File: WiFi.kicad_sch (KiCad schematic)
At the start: 0 parts

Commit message: PMIC DCDC
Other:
- title: Leaf RV1126 Power -> Leaf RV1126 PMIC RK809
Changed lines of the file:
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@@
   (paper "A4")
   (title_block
-    (title "Leaf RV1126 Power")
+    (title "Leaf RV1126 PMIC RK809")
     (date "2023-02-23")
     (rev "1")

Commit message: updated: PMIC codec
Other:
- title: Leaf RV1126 PMIC RK809 -> Leaf RV1126 PMIC RK809 Codec
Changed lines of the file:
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@@
   (paper "A4")
   (title_block
-    (title "Leaf RV1126 PMIC RK809")
-    (date "2023-02-23")
+    (title "Leaf RV1126 PMIC RK809 Codec")
+    (date "2023-02-25")
     (rev "1")
     (company "Qingdao IotPi Information Technology")

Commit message: updated: titles
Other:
- title: Leaf RV1126 PMIC RK809 Codec -> Leaf RV1126 RK809 WiFi
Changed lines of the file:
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@@
   (paper "A4")
   (title_block
-    (title "Leaf RV1126 PMIC RK809 Codec")
+    (title "Leaf RV1126 RK809 WiFi")
     (date "2023-02-25")
     (rev "1")

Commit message: added Wifi (AP6256)
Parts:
- added AE1: Antenna, symbol Device:Antenna
- added U9: AP6526, symbol Leaf_RF_Wifi:AP6256
- added Y2: Crystal, symbol Device:Crystal
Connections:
- new net ANTENNA: AE1.1 (A), U9.2 (WL_BT_ANT)
- new net GND: U9.1 (GND), U9.20 (GND), U9.3 (GND), U9.31 (GND), U9.33 (GND), U9.36 (GND)
- new net SDIO_CLK: U9.17 (SDIO_CLK)
- new net SDIO_CMD: U9.16 (SDIO_CMD)
- new net SDIO_D0: U9.18 (SDIO_D0)
- new net SDIO_D1: U9.19 (SDIO_D1)
- new net SDIO_D2: U9.14 (SDIO_D2)
- new net SDIO_D3: U9.15 (SDIO_D3)
- new net SDIO_VSEL: U9.29 (SDIO_VSEL)
- new net UART_RXD: U9.43 (UART_RXD)
- new net UART_TXD: U9.42 (UART_TXD)
- new net UART_~{CTS}: U9.44 (UART_~{CTS})
- new net UART_~{RTS}: U9.41 (UART_~{RTS})
- new net XTAL_IN: U9.10 (XTAL_IN), Y2.2
- new net XTAL_OUT: U9.11 (XTAL_OUT), Y2.1
- no-connect marks 0 -> 8

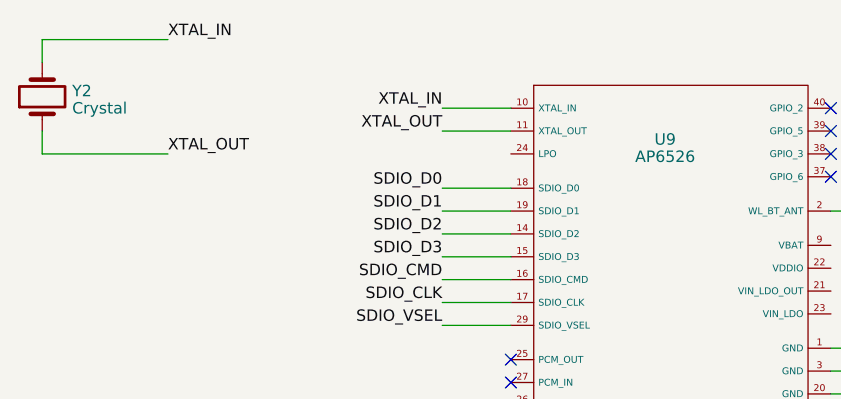
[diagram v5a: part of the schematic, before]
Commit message: updated footprints
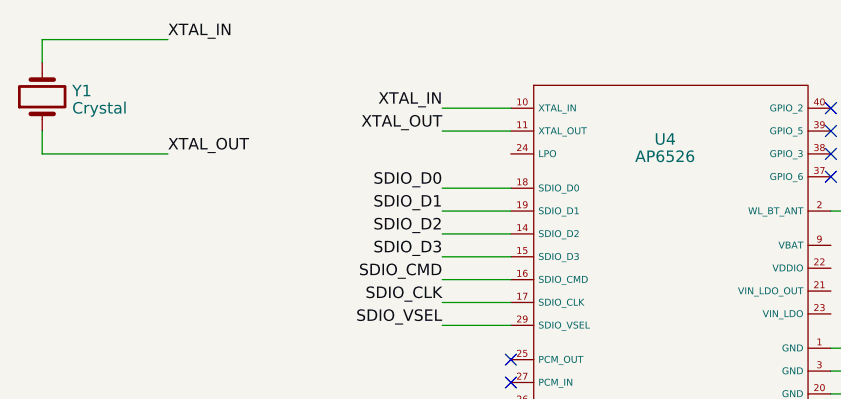
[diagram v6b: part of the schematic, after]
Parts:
- U4: renamed from U9; footprint (none) -> Leaf_RF_Module:QFN-44_12x12_Pitch0.9mm
- renumbered Y2 to Y1
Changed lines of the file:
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@@
   (symbol (lib_id "Device:Crystal") (at 78.74 41.91 90) (unit 1)
     (in_bom yes) (on_board yes) (dnp no) (fields_autoplaced)
-    (property "Reference" "Y2" (at 82.0674 41.2663 90)
+    (property "Reference" "Y1" (at 82.0674 41.2663 90)
       (effects (font (size 1.27 1.27)) (justify right))
     )
@@
       (project "leaf"
         (path "/e3b58043-16a3-43c8-9fad-9c9784eebfa4/cbba8301-b827-481f-8620-b434aac08349"
-          (reference "Y2") (unit 1)
+          (reference "Y1") (unit 1)
         )
       )
@@
   (symbol (lib_id "Leaf_RF_Wifi:AP6256") (at 148.59 73.66 0) (unit 1)
     (in_bom yes) (on_board yes) (dnp no) (fields_autoplaced)
-    (property "Reference" "U9" (at 147.955 46.6471 0)
+    (property "Reference" "U4" (at 147.955 46.6471 0)
       (effects (font (size 1.27 1.27)))
     )
@@
       (effects (font (size 1.27 1.27)))
     )
-    (property "Footprint" "" (at 147.955 59.69 0)
+    (property "Footprint" "Leaf_RF_Module:QFN-44_12x12_Pitch0.9mm" (at 147.955 59.69 0)
       (effects (font (size 1.27 1.27)) hide)
     )
@@
       (project "leaf"
         (path "/e3b58043-16a3-43c8-9fad-9c9784eebfa4/cbba8301-b827-481f-8620-b434aac08349"
-          (reference "U9") (unit 1)
+          (reference "U4") (unit 1)
         )
       )
@@
   (symbol (lib_id "power:GND") (at 176.53 86.36 0) (unit 1)
     (in_bom yes) (on_board yes) (dnp no) (fields_autoplaced)
-    (property "Reference" "#PWR056" (at 176.53 92.71 0)
+    (property "Reference" "#PWR045" (at 176.53 92.71 0)
       (effects (font (size 1.27 1.27)) hide)
     )
@@
       (project "leaf"
         (path "/e3b58043-16a3-43c8-9fad-9c9784eebfa4/cbba8301-b827-481f-8620-b434aac08349"
-          (reference "#PWR056") (unit 1)
+          (reference "#PWR045") (unit 1)
         )
       )

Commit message: updated Reference, and PCB
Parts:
- removed AE1: Antenna, symbol Device:Antenna
- added AE1: Antenna_Chip, RF_Antenna:Johanson_2450AT18x100, symbol Device:Antenna_Chip
- added C151: 100nF, Capacitor_SMD:C_0201_0603Metric, symbol Device:C
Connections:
- net ANTENNA: now also AE1.1 (FEED)
- net GND: now also C151.2
- new net: AE1.2 (PCB_Trace), C151.1
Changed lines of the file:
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@@
+    (stroke (width 0) (type default))
+  )
+  (wire (pts (xy 237.49 50.8) (xy 237.49 53.34))
     (stroke (width 0) (type default))
   )
@@
   )
   (wire (pts (xy 166.37 69.85) (xy 176.53 69.85))
+    (stroke (width 0) (type default))
+  )
+  (wire (pts (xy 237.49 60.96) (xy 237.49 63.5))
     (stroke (width 0) (type default))
   )
@@
     )
   )
+  (symbol (lib_id "Device:Antenna_Chip") (at 234.95 48.26 0) (unit 1)
+    (in_bom yes) (on_board yes) (dnp no) (fields_autoplaced)
+    (property "Reference" "AE1" (at 239.522 45.0763 0)
+      (effects (font (size 1.27 1.27)) (justify left))
+    )
+    (property "Value" "Antenna_Chip" (at 239.522 46.9973 0)
+      (effects (font (size 1.27 1.27)) (justify left))
+    )
+    (property "Footprint" "RF_Antenna:Johanson_2450AT18x100" (at 232.41 43.815 0)
+      (effects (font (size 1.27 1.27)) hide)
+    )
+    (property "Datasheet" "~" (at 232.41 43.815 0)
+      (effects (font (size 1.27 1.27)) hide)
+    )
+    (pin "1")
+    (pin "2")
+    (instances
+      (project "leaf"
+        (path "/e3b58043-16a3-43c8-9fad-9c9784eebfa4/cbba8301-b827-481f-8620-b434aac08349"
+          (reference "AE1") (unit 1)
+        )
+      )
+    )
+  )
+  (symbol (lib_id "power:GND") (at 237.49 63.5 0) (unit 1)
+    (in_bom yes) (on_board yes) (dnp no) (fields_autoplaced)
+    (property "Reference" "#PWR0136" (at 237.49 69.85 0)
+      (effects (font (size 1.27 1.27)) hide)
+    )
+    (property "Value" "GND" (at 237.49 67.6355 0)
+      (effects (font (size 1.27 1.27)))
+    )
+    (property "Footprint" "" (at 237.49 63.5 0)
+      (effects (font (size 1.27 1.27)) hide)
+    )
+    (property "Datasheet" "" (at 237.49 63.5 0)
+      (effects (font (size 1.27 1.27)) hide)
+    )
+    (pin "1")
+    (instances
+      (project "leaf"
+        (path "/e3b58043-16a3-43c8-9fad-9c9784eebfa4/cbba8301-b827-481f-8620-b434aac08349"
+          (reference "#PWR0136") (unit 1)
+        )
+      )
+    )
+  )
+  (symbol (lib_id "Device:C") (at 237.49 57.15 0) (unit 1)
+    (in_bom yes) (on_board yes) (dnp no) (fields_autoplaced)
+    (property "Reference" "C151" (at 240.411 56.5063 0)
+      (effects (font (size 1.27 1.27)) (justify left))
+    )
+    (property "Value" "100nF" (at 240.411 58.4273 0)
+      (effects (font (size 1.27 1.27)) (justify left))
+    )
+    (property "Footprint" "Capacitor_SMD:C_0201_0603Metric" (at 238.4552 60.96 0)
+      (effects (font (size 1.27 1.27)) hide)
+    )
+    (property "Datasheet" "~" (at 237.49 57.15 0)
+      (effects (font (size 1.27 1.27)) hide)
+    )
+    (pin "1")
+    (pin "2")
+    (instances
+      (project "leaf"
+        (path "/e3b58043-16a3-43c8-9fad-9c9784eebfa4/cbba8301-b827-481f-8620-b434aac08349"
+          (reference "C151") (unit 1)
+        )
+      )
+    )
+  )
   (symbol (lib_id "power:GND") (at 176.53 86.36 0) (unit 1)
     (in_bom yes) (on_board yes) (dnp no) (fields_autoplaced)
@@
         )
       )
-    )
-  )
-  (symbol (lib_id "Device:Antenna") (at 232.41 45.72 0) (unit 1)
-    (in_bom yes) (on_board yes) (dnp no) (fields_autoplaced)
-    (property "Reference" "AE1" (at 234.442 45.7113 0)
-      (effects (font (size 1.27 1.27)) (justify left))
-    )
-    (property "Value" "Antenna" (at 234.442 47.6323 0)
-      (effects (font (size 1.27 1.27)) (justify left))
-    )
-    (property "Footprint" "" (at 232.41 45.72 0)
-      (effects (font (size 1.27 1.27)) hide)
-    )
-    (property "Datasheet" "~" (at 232.41 45.72 0)
-      (effects (font (size 1.27 1.27)) hide)
-    )
-    (pin "1")
-    (instances
-      (project "leaf"
-        (path "/e3b58043-16a3-43c8-9fad-9c9784eebfa4/cbba8301-b827-481f-8620-b434aac08349"
-          (reference "AE1") (unit 1)
-        )
-      )

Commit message: remove WiFI module
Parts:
- U4: now left out of the parts list
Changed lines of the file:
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@@
   )
   (symbol (lib_id "Leaf_RF_Wifi:AP6256") (at 148.59 73.66 0) (unit 1)
-    (in_bom yes) (on_board yes) (dnp no) (fields_autoplaced)
+    (in_bom no) (on_board no) (dnp no) (fields_autoplaced)
     (property "Reference" "U4" (at 147.955 46.6471 0)
       (effects (font (size 1.27 1.27)))
